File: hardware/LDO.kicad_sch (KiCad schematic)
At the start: 5 parts, among them U1 MCP1826S

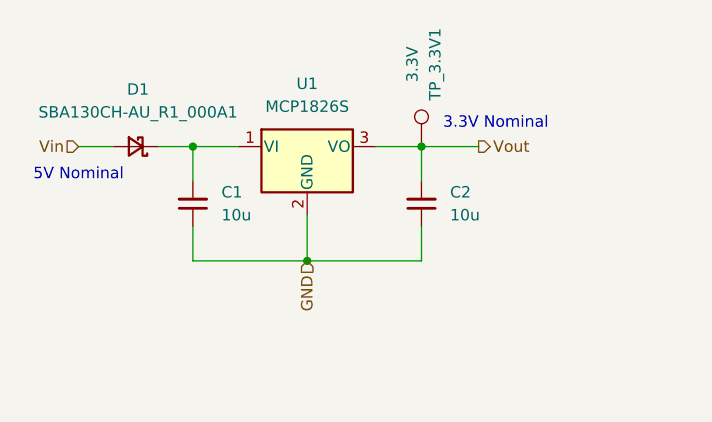
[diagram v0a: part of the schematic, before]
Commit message: labeled + stm32 cube layout
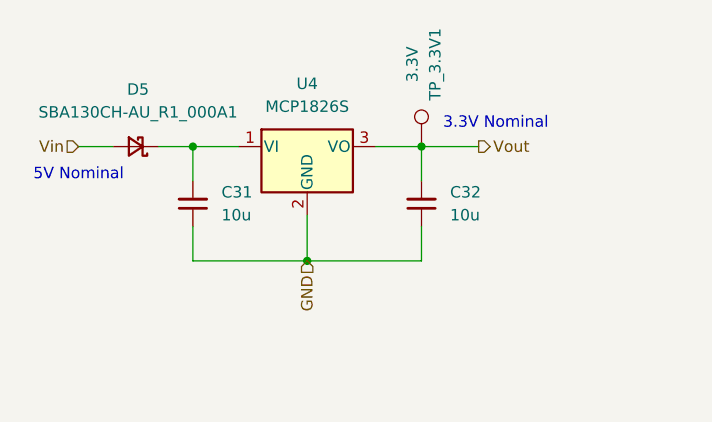
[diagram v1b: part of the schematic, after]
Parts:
- removed C1, C2: 10u, Capacitor_SMD:C_0805_2012Metric_Pad1.18x1.45mm_HandSolder, symbol Device:C_Small
- removed D1: SBA130CH-AU_R1_000A1, Diode_SMD:D_SOD-323_HandSoldering, symbol Device:D_Schottky_Small
- removed U1: MCP1826S, Package_TO_SOT_SMD:SOT-223-3_TabPin2, symbol Regulator_Linear:MCP1826S
- added C31, C32: 10u, Capacitor_SMD:C_0805_2012Metric_Pad1.18x1.45mm_HandSolder, symbol Device:C_Small
- added D5: SBA130CH-AU_R1_000A1, Diode_SMD:D_SOD-323_HandSoldering, symbol Device:D_Schottky_Small
- added U4: MCP1826S, Package_TO_SOT_SMD:SOT-223-3_TabPin2, symbol Regulator_Linear:MCP1826S
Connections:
- net GND: now also C31.1, C32.1, U4.2 (GND)
- net Vin: now also D5.2 (A)
- net Vout: now also C32.2, U4.3 (VO)
- new net: C31.2, D5.1 (K), U4.1 (VI)
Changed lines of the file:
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@@
+		)
+	)
+	(hierarchical_label "Vin"
+		(shape input)
+		(at 127 63.5 180)
+		(effects
+			(font
+				(size 1.27 1.27)
+			)
+			(justify right)
 		)
 	)
@@
 		)
 	)
-	(hierarchical_label "Vin"
-		(shape input)
-		(at 127 63.5 180)
-		(effects
-			(font
-				(size 1.27 1.27)
-			)
-			(justify right)
-		)
-	)
 	(hierarchical_label "Vout"
 		(shape output)
@@
 			)
 			(justify left)
+		)
+	)
+	(symbol
+		(lib_id "Device:D_Schottky_Small")
+		(at 133.35 63.5 180)
+		(unit 1)
+		(exclude_from_sim no)
+		(in_bom yes)
+		(on_board yes)
+		(dnp no)
+		(fields_autoplaced yes)
+		(property "Reference" "D5"
+			(at 133.604 57.15 0)
+			(effects
+				(font
+					(size 1.27 1.27)
+				)
+			)
+		)
+		(property "Value" "SBA130CH-AU_R1_000A1"
+			(at 133.604 59.69 0)
+			(effects
+				(font
+					(size 1.27 1.27)
+				)
+			)
+		)
+		(property "Footprint" "Diode_SMD:D_SOD-323_HandSoldering"
+			(at 133.35 63.5 90)
+			(effects
+				(font
+					(size 1.27 1.27)
+				)
+				(hide yes)
+			)
+		)
+		(property "Datasheet" "https://www.mouser.com/datasheet/3/3736/1/11145663EF9055F8C188C22CC003165FC5A818A8439A953D3A6E1D8FCBF51DA1.pdf"
+			(at 133.35 63.5 90)
+			(effects
+				(font
+					(size 1.27 1.27)
+				)
+				(hide yes)
+			)
+		)
+		(property "Description" "Schottky diode, small symbol"
+			(at 133.35 63.5 0)
+			(effects
+				(font
+					(size 1.27 1.27)
+				)
+				(hide yes)
+			)
+		)
+		(property "LCSC P/N" "C191023"
+			(at 133.35 63.5 0)
+			(effects
+				(font
+					(size 1.27 1.27)
+				)
+				(hide yes)
+			)
+		)
+		(property "P/N" "SBA130CH-AU_R1_000A1 "
+			(at 133.35 63.5 0)
+			(effects
+				(font
+					(size 1.27 1.27)
+				)
+				(hide yes)
+			)
+		)
+		(property "Old P/N" "BAT760-7"
+			(at 133.35 63.5 0)
+			(effects
+				(font
+					(size 1.27 1.27)
+				)
+				(hide yes)
+			)
+		)
+		(property "Old LCSC P/N" "C124187"
+			(at 133.35 63.5 0)
+			(effects
+				(font
+					(size 1.27 1.27)
+				)
+				(hide yes)
+			)
+		)
+		(pin "1"
+		)
+		(pin "2"
+		)
+		(instances
+			(project ""
+				(path "/2365a867-6254-4a7c-9718-f325e0bbac5c/904fa10a-747c-46cf-90d1-33d76069dc5d/d9c02800-502d-4b66-a933-6a0fcb4cc3ad"
+					(reference "D5")
+					(unit 1)
+				)
+			)
+			(project ""
+				(path "/8ff43370-8d10-4d2c-b1a3-81d1c2934a98"
+					(reference "D1")
+					(unit 1)
+				)
+			)
 		)
 	)
@@
 		(dnp no)
 		(fields_autoplaced yes)
-		(property "Reference" "C2"
+		(property "Reference" "C32"
 			(at 168.275 68.5735 0)
 			(effects
@@
 			(project "LDO"
 				(path "/2365a867-6254-4a7c-9718-f325e0bbac5c/904fa10a-747c-46cf-90d1-33d76069dc5d/d9c02800-502d-4b66-a933-6a0fcb4cc3ad"
-					(reference "C2")
+					(reference "C32")
 					(unit 1)
 				)
@@
 		(dnp no)
 		(fields_autoplaced yes)
-		(property "Reference" "U1"
+		(property "Reference" "U4"
 			(at 152.4 56.515 0)
 			(effects
@@
 			(project ""
 				(path "/2365a867-6254-4a7c-9718-f325e0bbac5c/904fa10a-747c-46cf-90d1-33d76069dc5d/d9c02800-502d-4b66-a933-6a0fcb4cc3ad"
-					(reference "U1")
+					(reference "U4")
 					(unit 1)
 				)
@@
 				(path "/8ff43370-8d10-4d2c-b1a3-81d1c2934a98"
 					(reference "U1")
-					(unit 1)
-				)
-			)
-		)
-	)
-	(symbol
-		(lib_id "Device:D_Schottky_Small")
-		(at 133.35 63.5 180)
-		(unit 1)
-		(exclude_from_sim no)
-		(in_bom yes)
-		(on_board yes)
-		(dnp no)
-		(fields_autoplaced yes)
-		(property "Reference" "D1"
-			(at 133.604 57.15 0)
-			(effects
-				(font
-					(size 1.27 1.27)
-				)
-			)
-		)
-		(property "Value" "SBA130CH-AU_R1_000A1"
-			(at 133.604 59.69 0)
-			(effects
-				(font
-					(size 1.27 1.27)
-				)
-			)
-		)
-		(property "Footprint" "Diode_SMD:D_SOD-323_HandSoldering"
-			(at 133.35 63.5 90)
-			(effects
-				(font
-					(size 1.27 1.27)
-				)
-				(hide yes)
-			)
-		)
-		(property "Datasheet" "https://www.mouser.com/datasheet/3/3736/1/11145663EF9055F8C188C22CC003165FC5A818A8439A953D3A6E1D8FCBF51DA1.pdf"
-			(at 133.35 63.5 90)
-			(effects
-				(font
-					(size 1.27 1.27)
-				)
-				(hide yes)
-			)
-		)
-		(property "Description" "Schottky diode, small symbol"
-			(at 133.35 63.5 0)
-			(effects
-				(font
-					(size 1.27 1.27)
-				)
-				(hide yes)
-			)
-		)
-		(property "LCSC P/N" "C191023"
-			(at 133.35 63.5 0)
-			(effects
-				(font
-					(size 1.27 1.27)
-				)
-				(hide yes)
-			)
-		)
-		(property "P/N" "SBA130CH-AU_R1_000A1 "
-			(at 133.35 63.5 0)
-			(effects
-				(font
-					(size 1.27 1.27)
-				)
-				(hide yes)
-			)
-		)
-		(property "Old P/N" "BAT760-7"
-			(at 133.35 63.5 0)
-			(effects
-				(font
-					(size 1.27 1.27)
-				)
-				(hide yes)
-			)
-		)
-		(property "Old LCSC P/N" "C124187"
-			(at 133.35 63.5 0)
-			(effects
-				(font
-					(size 1.27 1.27)
-				)
-				(hide yes)
-			)
-		)
-		(pin "1"
-		)
-		(pin "2"
-		)
-		(instances
-			(project ""
-				(path "/2365a867-6254-4a7c-9718-f325e0bbac5c/904fa10a-747c-46cf-90d1-33d76069dc5d/d9c02800-502d-4b66-a933-6a0fcb4cc3ad"
-					(reference "D1")
-					(unit 1)
-				)
-			)
-			(project ""
-				(path "/8ff43370-8d10-4d2c-b1a3-81d1c2934a98"
-					(reference "D1")
 					(unit 1)
 				)
@@
 		(dnp no)
 		(fields_autoplaced yes)
-		(property "Reference" "C1"
+		(property "Reference" "C31"
 			(at 142.875 68.5735 0)
 			(effects
@@
 			(project "LDO"
 				(path "/2365a867-6254-4a7c-9718-f325e0bbac5c/904fa10a-747c-46cf-90d1-33d76069dc5d/d9c02800-502d-4b66-a933-6a0fcb4cc3ad"
-					(reference "C1")
-					(unit 1)
-				)
+					(reference "C31")
+					(unit 1)
+				)

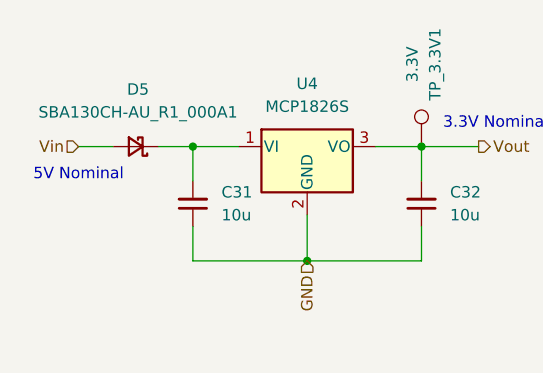
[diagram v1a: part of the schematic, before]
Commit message: added debug led
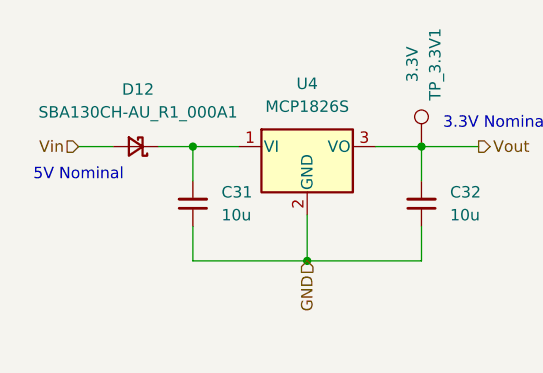
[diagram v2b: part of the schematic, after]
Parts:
- renumbered D5 to D12
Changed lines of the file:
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@@
 		(dnp no)
 		(fields_autoplaced yes)
-		(property "Reference" "D5"
+		(property "Reference" "D12"
 			(at 133.604 57.15 0)
 			(effects
@@
 			(project ""
 				(path "/2365a867-6254-4a7c-9718-f325e0bbac5c/904fa10a-747c-46cf-90d1-33d76069dc5d/d9c02800-502d-4b66-a933-6a0fcb4cc3ad"
-					(reference "D5")
+					(reference "D12")
 					(unit 1)
 				)

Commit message: added calcs, cleaned up, addressed comments
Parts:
- renumbered C31 to C6, C32 to C7, D12 to D7, U4 to U1
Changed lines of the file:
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@@
 		(dnp no)
 		(fields_autoplaced yes)
-		(property "Reference" "D12"
+		(property "Reference" "D7"
 			(at 133.604 57.15 0)
 			(show_name no)
@@
 			(project "PS-HVCarrier"
 				(path "/2365a867-6254-4a7c-9718-f325e0bbac5c/904fa10a-747c-46cf-90d1-33d76069dc5d/d9c02800-502d-4b66-a933-6a0fcb4cc3ad"
-					(reference "D12")
+					(reference "D7")
 					(unit 1)
 				)
@@
 		(dnp no)
 		(fields_autoplaced yes)
-		(property "Reference" "C32"
+		(property "Reference" "C7"
 			(at 168.275 68.5735 0)
 			(show_name no)
@@
 			(project "PS-HVCarrier"
 				(path "/2365a867-6254-4a7c-9718-f325e0bbac5c/904fa10a-747c-46cf-90d1-33d76069dc5d/d9c02800-502d-4b66-a933-6a0fcb4cc3ad"
-					(reference "C32")
+					(reference "C7")
 					(unit 1)
 				)
@@
 		(dnp no)
 		(fields_autoplaced yes)
-		(property "Reference" "U4"
+		(property "Reference" "U1"
 			(at 152.4 56.515 0)
 			(show_name no)
@@
 			)
 		)
-		(property "Datasheet" "http://ww1.microchip.com/downloads/en/DeviceDoc/22057B.pdf"
+		(property "Datasheet" "kicad-embed://MCP1826S.pdf"
 			(at 152.4 57.15 0)
 			(hide yes)
@@
 			(project "PS-HVCarrier"
 				(path "/2365a867-6254-4a7c-9718-f325e0bbac5c/904fa10a-747c-46cf-90d1-33d76069dc5d/d9c02800-502d-4b66-a933-6a0fcb4cc3ad"
-					(reference "U4")
+					(reference "U1")
 					(unit 1)
 				)
@@
 		(dnp no)
 		(fields_autoplaced yes)
-		(property "Reference" "C31"
+		(property "Reference" "C6"
 			(at 142.875 68.5735 0)
 			(show_name no)
@@
 			(project "PS-HVCarrier"
 				(path "/2365a867-6254-4a7c-9718-f325e0bbac5c/904fa10a-747c-46cf-90d1-33d76069dc5d/d9c02800-502d-4b66-a933-6a0fcb4cc3ad"
-					(reference "C31")
-					(unit 1)
-				)
+					(reference "C6")
+					(unit 1)
+				)
